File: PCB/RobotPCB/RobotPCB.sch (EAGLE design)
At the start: 45 parts, among them IC1 MPU6050, IC2 MCP73831/OT, U1 DRV8835, U2 CP2104-F03-GM

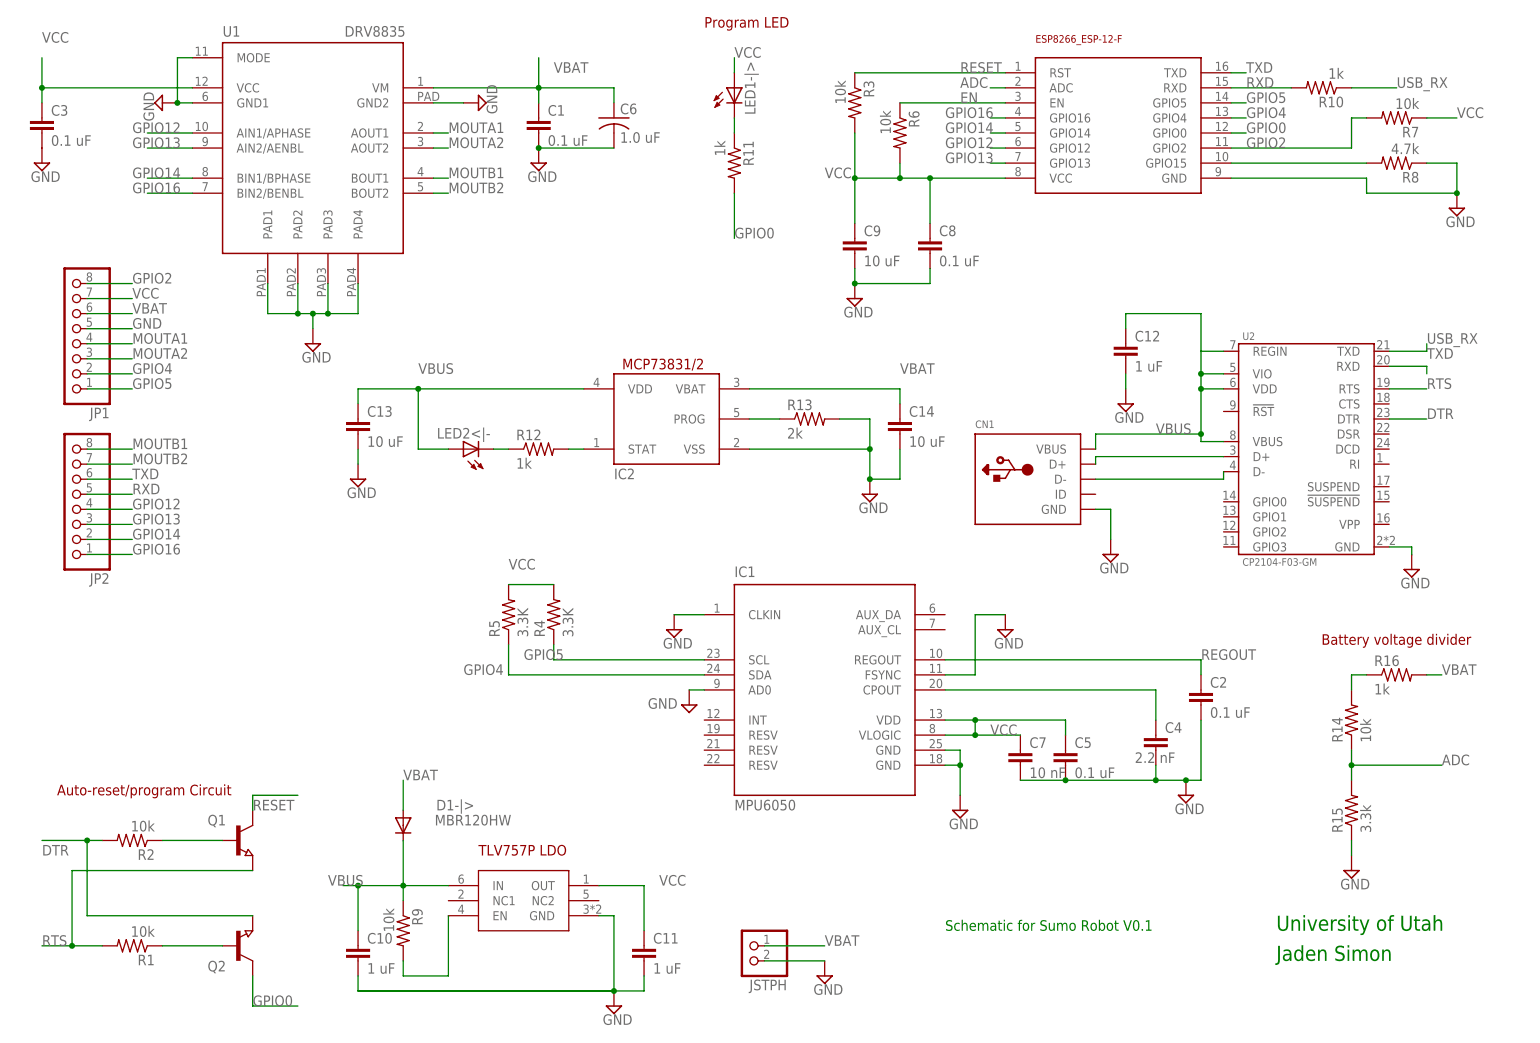
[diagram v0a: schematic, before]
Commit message: Optimized Robot PCB
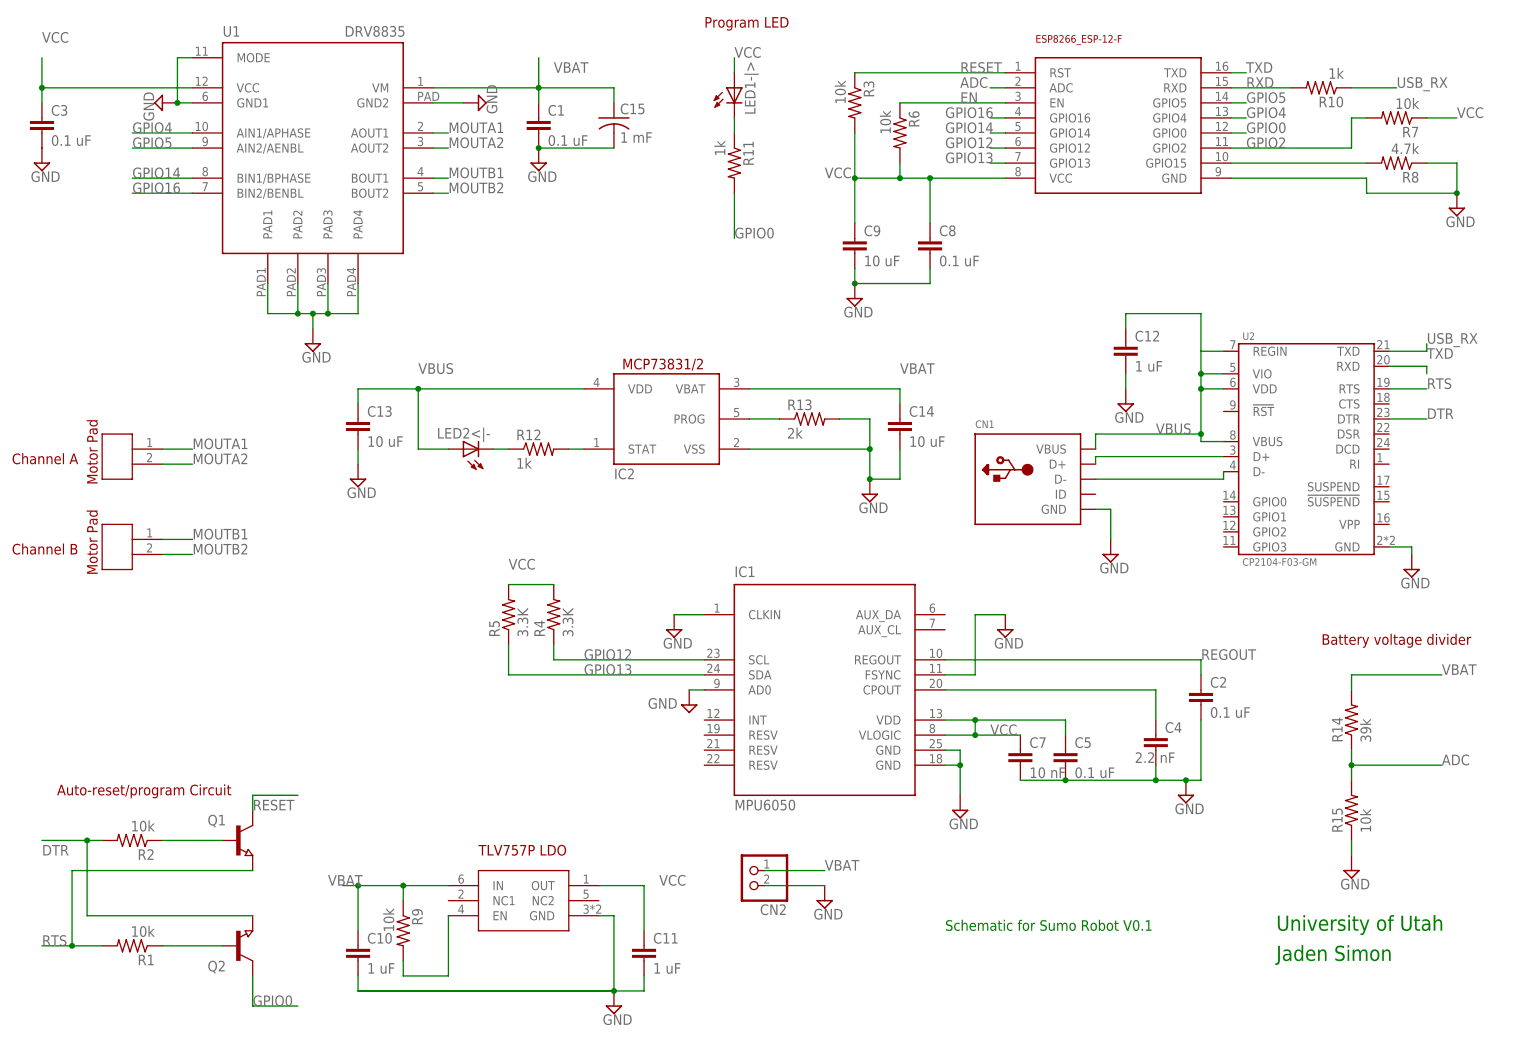
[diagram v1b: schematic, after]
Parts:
- removed C6: 1.0 uF, rcl:C-US025-050X050
- removed D1-|>: MBR120HW, diode:MBR0520LT
- removed JP1, JP2: (no value), pinhead:PINHD-1X8
- removed JSTPH: (no value), adafruit:JST_2PIN-SMT-RA
- removed R16: 1k, rcl:R-US_M1206
- added C15: 1 mF, rcl:C-US050-075X075
- added CN2: (no value), adafruit:JST_2PIN-THM
- added U$3, U$4: MOTOR_PAD, ECE5780-MotorDriver:MOTOR_PAD
- R14: value 10k -> 39k
- R15: value 3.3k -> 10k
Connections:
- removed net N$6: R14.2, R16.1
- net GND: now also C15.2, CN2.1; no longer C6.2, JP1.5, JSTPH.1
- net GPIO12: now also IC1G$1.SCL, R4.1; no longer JP2.4, U1.AIN1/APHASE
- net GPIO13: now also IC1G$1.SDA, R5.1; no longer JP2.3, U1.AIN2/AENBL
- net GPIO14: no longer JP2.2
- net GPIO16: no longer JP2.1
- net GPIO2: no longer JP1.8
- net GPIO4: now also U1.AIN1/APHASE; no longer IC1G$1.SDA, JP1.2, R5.1
- net GPIO5: now also U1.AIN2/AENBL; no longer IC1G$1.SCL, JP1.1, R4.1
- net MOUTA1: now also U$3.L; no longer JP1.4
- net MOUTA2: now also U$3.2; no longer JP1.3
- net MOUTB1: now also U$4.L; no longer JP2.8
- net MOUTB2: now also U$4.2; no longer JP2.7
- net RXD: no longer JP2.5
- net TXD: no longer JP2.6
- net VBAT: now also C10.1, C15.1, CN2.2, R14.2, R9.1, U$2.IN; no longer C6.1, D1-|>.A, JP1.6, JSTPH.2, R16.2
- net VBUS: no longer C10.1, D1-|>.C, R9.1, U$2.IN
- net VCC: no longer JP1.7
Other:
- note added: "Channel A"
- note added: "Channel B"

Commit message: Fixed PCB mounting holes
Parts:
- R14: value 39k -> 33k
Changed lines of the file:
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@@
 <part name="SUPPLY19" library="supply2" library_urn="urn:adsk.eagle:library:372" deviceset="GND" device=""/>
 <part name="Q2" library="semicon-smd-ipc" library_urn="urn:adsk.eagle:library:353" deviceset="NPN-TRANSISTOR_" device="SOT23" package3d_urn="urn:adsk.eagle:package:26310/1"/>
-<part name="R14" library="rcl" library_urn="urn:adsk.eagle:library:334" deviceset="R-US_" device="M1206" package3d_urn="urn:adsk.eagle:package:23566/1" value="39k"/>
+<part name="R14" library="rcl" library_urn="urn:adsk.eagle:library:334" deviceset="R-US_" device="M1206" package3d_urn="urn:adsk.eagle:package:23566/1" value="33k"/>
 <part name="R15" library="rcl" library_urn="urn:adsk.eagle:library:334" deviceset="R-US_" device="M1206" package3d_urn="urn:adsk.eagle:package:23566/1" value="10k"/>
 <part name="SUPPLY20" library="supply2" library_urn="urn:adsk.eagle:library:372" deviceset="GND" device=""/>

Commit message: Finalized Robot PCB
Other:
- moved on the sheet: U1
